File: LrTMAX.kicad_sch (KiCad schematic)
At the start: 126 parts, among them J1 USB_C_Receptacle_USB2.0, J2 Conn_02x05_Odd_Even, Q1 2N7002, SW1 Tact_SW_8mm, SW10 EC11_SMD, SW11 EC11_SMD, SW12 EC11_SMD, SW13 EC11_SMD, SW14 EC11_SMD, SW15 EC11_SMD, SW16 EC11_SMD, SW17 EC11_SMD, SW2 Tact_SW_8mm, SW20 SW_SPST, SW3 Tact_SW_8mm, SW4 Tact_SW_8mm, SW5 Tact_SW_8mm, SW6 Tact_SW_8mm, SW7 Tact_SW_8mm, SW8 Tact_SW_8mm, U1 STM32F072C8Tx, U3 SSD1306_OLED_0.91, U4 SPX3819M5-L3-3TR

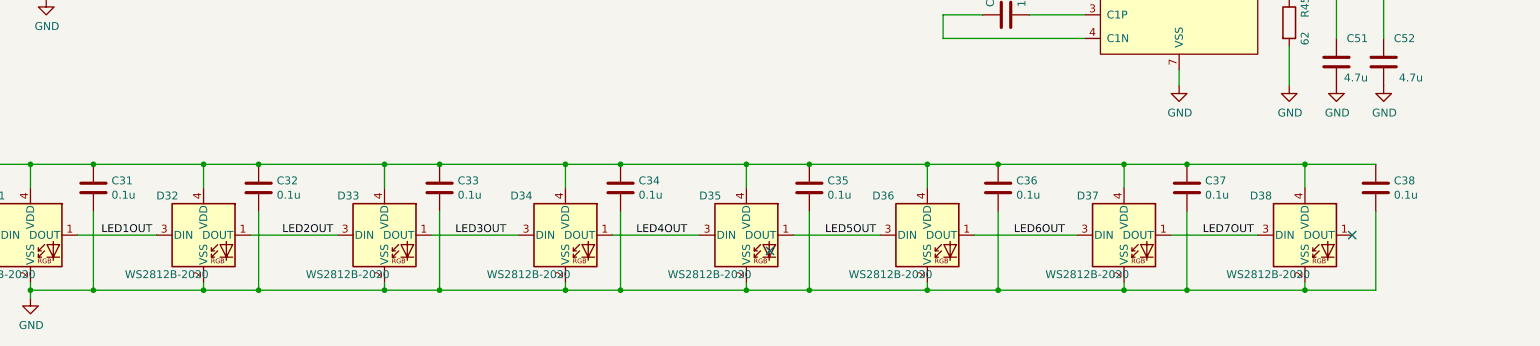
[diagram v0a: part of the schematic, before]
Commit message: change schematic 0.1->100n
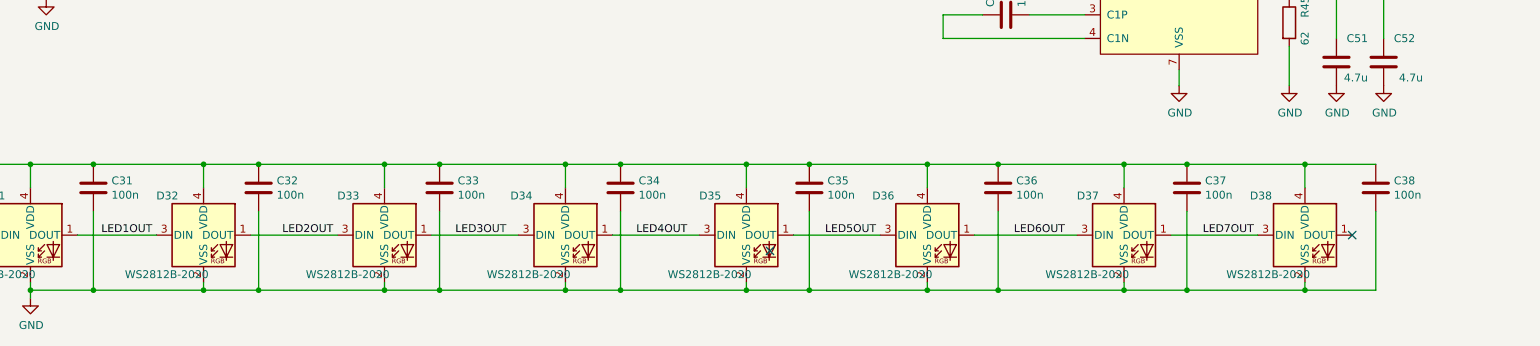
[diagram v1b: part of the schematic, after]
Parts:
- C31, C32, C33, C34, C35, C36, C37, C38: value 0.1u -> 100n
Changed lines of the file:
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@@
       (effects (font (size 1.27 1.27)) (justify left))
     )
-    (property "Value" "0.1u" (id 1) (at 53.721 262.763 0)
+    (property "Value" "100n" (id 1) (at 53.721 262.763 0)
       (effects (font (size 1.27 1.27)) (justify left))
     )
@@
       (effects (font (size 1.27 1.27)) (justify left))
     )
-    (property "Value" "0.1u" (id 1) (at 80.391 262.763 0)
+    (property "Value" "100n" (id 1) (at 80.391 262.763 0)
       (effects (font (size 1.27 1.27)) (justify left))
     )
@@
       (effects (font (size 1.27 1.27)) (justify left))
     )
-    (property "Value" "0.1u" (id 1) (at 109.601 262.763 0)
+    (property "Value" "100n" (id 1) (at 109.601 262.763 0)
       (effects (font (size 1.27 1.27)) (justify left))
     )
@@
       (effects (font (size 1.27 1.27)) (justify left))
     )
-    (property "Value" "0.1u" (id 1) (at 138.811 262.763 0)
+    (property "Value" "100n" (id 1) (at 138.811 262.763 0)
       (effects (font (size 1.27 1.27)) (justify left))
     )
@@
       (effects (font (size 1.27 1.27)) (justify left))
     )
-    (property "Value" "0.1u" (id 1) (at 169.291 262.763 0)
+    (property "Value" "100n" (id 1) (at 169.291 262.763 0)
       (effects (font (size 1.27 1.27)) (justify left))
     )
@@
       (effects (font (size 1.27 1.27)) (justify left))
     )
-    (property "Value" "0.1u" (id 1) (at 199.771 262.763 0)
+    (property "Value" "100n" (id 1) (at 199.771 262.763 0)
       (effects (font (size 1.27 1.27)) (justify left))
     )
@@
       (effects (font (size 1.27 1.27)) (justify left))
     )
-    (property "Value" "0.1u" (id 1) (at 230.251 262.763 0)
+    (property "Value" "100n" (id 1) (at 230.251 262.763 0)
       (effects (font (size 1.27 1.27)) (justify left))
     )
@@
       (effects (font (size 1.27 1.27)) (justify left))
     )
-    (property "Value" "0.1u" (id 1) (at 260.731 262.763 0)
+    (property "Value" "100n" (id 1) (at 260.731 262.763 0)
       (effects (font (size 1.27 1.27)) (justify left))
     )
@@
     )
     (path "/00000000-0000-0000-0000-00005d7055e7"
-      (reference "C31") (unit 1) (value "0.1u") (footprint "Capacitor_SMD:C_0805_2012Metric")
+      (reference "C31") (unit 1) (value "100n") (footprint "Capacitor_SMD:C_0805_2012Metric")
     )
     (path "/00000000-0000-0000-0000-00005d706229"
-      (reference "C32") (unit 1) (value "0.1u") (footprint "Capacitor_SMD:C_0805_2012Metric")
+      (reference "C32") (unit 1) (value "100n") (footprint "Capacitor_SMD:C_0805_2012Metric")
     )
     (path "/00000000-0000-0000-0000-00005d706b4b"
-      (reference "C33") (unit 1) (value "0.1u") (footprint "Capacitor_SMD:C_0805_2012Metric")
+      (reference "C33") (unit 1) (value "100n") (footprint "Capacitor_SMD:C_0805_2012Metric")
     )
     (path "/00000000-0000-0000-0000-00005d707270"
-      (reference "C34") (unit 1) (value "0.1u") (footprint "Capacitor_SMD:C_0805_2012Metric")
+      (reference "C34") (unit 1) (value "100n") (footprint "Capacitor_SMD:C_0805_2012Metric")
     )
     (path "/00000000-0000-0000-0000-00005d7076c0"
-      (reference "C35") (unit 1) (value "0.1u") (footprint "Capacitor_SMD:C_0805_2012Metric")
+      (reference "C35") (unit 1) (value "100n") (footprint "Capacitor_SMD:C_0805_2012Metric")
     )
     (path "/00000000-0000-0000-0000-00005d708e26"
-      (reference "C36") (unit 1) (value "0.1u") (footprint "Capacitor_SMD:C_0805_2012Metric")
+      (reference "C36") (unit 1) (value "100n") (footprint "Capacitor_SMD:C_0805_2012Metric")
     )
     (path "/00000000-0000-0000-0000-000060809be9"
-      (reference "C37") (unit 1) (value "0.1u") (footprint "Capacitor_SMD:C_0805_2012Metric")
+      (reference "C37") (unit 1) (value "100n") (footprint "Capacitor_SMD:C_0805_2012Metric")
     )
     (path "/00000000-0000-0000-0000-000060809bf1"
-      (reference "C38") (unit 1) (value "0.1u") (footprint "Capacitor_SMD:C_0805_2012Metric")
+      (reference "C38") (unit 1) (value "100n") (footprint "Capacitor_SMD:C_0805_2012Metric")
     )
     (path "/00000000-0000-0000-0000-00005c490efe"

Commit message: some pattern/sylk refinement
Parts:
- C10, C11, C12, C13, C14, C15, C16, C17, C18, C19, C20, C21, C22, C23, C24, C25: value 22n -> 33n
- H1, H2, H3, H4: now left out of the parts list
- R48: value 1K -> 470
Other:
- note added: "LrTMAX type C/DFU/SSM"
- note removed: "LrTMAX type C/DFU"
- title: LrTMAX 1.2d -> LrTMAX 1.2
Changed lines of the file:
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@@
   (paper "A3")
   (title_block
-    (title "LrTMAX 1.2d")
+    (title "LrTMAX 1.2")
     (date "2019-01-24")
     (company "Ruffles Inc,.")
@@
     (stroke (width 0) (type default) (color 0 0 0 0))
   )
-  (text "LrTMAX type C/DFU" (at 330.2 265.43 0)
+  (text "LrTMAX type C/DFU/SSM" (at 308.61 264.16 0)
     (effects (font (size 5.0038 5.0038)) (justify left bottom))
   )
@@
   )
   (symbol (lib_id "LrE-6-rescue:MountingHole-Mechanical") (at 307.34 247.65 0) (unit 1)
-    (in_bom yes) (on_board yes)
+    (in_bom no) (on_board yes)
     (property "Reference" "H1" (id 0) (at 309.88 246.4816 0)
       (effects (font (size 1.27 1.27)) (justify left))
@@
   )
   (symbol (lib_id "LrE-6-rescue:MountingHole-Mechanical") (at 328.93 247.65 0) (unit 1)
-    (in_bom yes) (on_board yes)
+    (in_bom no) (on_board yes)
     (property "Reference" "H2" (id 0) (at 331.47 246.4816 0)
       (effects (font (size 1.27 1.27)) (justify left))
@@
   )
   (symbol (lib_id "LrE-6-rescue:MountingHole-Mechanical") (at 349.25 247.65 0) (unit 1)
-    (in_bom yes) (on_board yes)
+    (in_bom no) (on_board yes)
     (property "Reference" "H3" (id 0) (at 351.79 246.4816 0)
       (effects (font (size 1.27 1.27)) (justify left))
@@
   )
   (symbol (lib_id "LrE-6-rescue:MountingHole-Mechanical") (at 370.84 247.65 0) (unit 1)
-    (in_bom yes) (on_board yes)
+    (in_bom no) (on_board yes)
     (property "Reference" "H4" (id 0) (at 373.38 246.4816 0)
       (effects (font (size 1.27 1.27)) (justify left))
@@
     (in_bom yes) (on_board yes)
     (property "Reference" "R48" (id 0) (at 60.96 205.5622 90))
-    (property "Value" "1K" (id 1) (at 60.96 207.8736 90))
+    (property "Value" "470" (id 1) (at 60.96 207.8736 90))
     (property "Footprint" "Resistor_SMD:R_0805_2012Metric" (id 2) (at 60.96 209.042 90)
       (effects (font (size 1.27 1.27)) hide)
@@
       (effects (font (size 1.27 1.27)) (justify left))
     )
-    (property "Value" "22n" (id 1) (at 40.64 90.17 0)
+    (property "Value" "33n" (id 1) (at 40.64 90.17 0)
       (effects (font (size 1.27 1.27)) (justify left))
     )
@@
       (effects (font (size 1.27 1.27)) (justify left))
     )
-    (property "Value" "22n" (id 1) (at 49.53 90.17 0)
+    (property "Value" "33n" (id 1) (at 49.53 90.17 0)
       (effects (font (size 1.27 1.27)) (justify left))
     )
@@
       (effects (font (size 1.27 1.27)) (justify left))
     )
-    (property "Value" "22n" (id 1) (at 39.37 132.08 0)
+    (property "Value" "33n" (id 1) (at 39.37 132.08 0)
       (effects (font (size 1.27 1.27)) (justify left))
     )
@@
       (effects (font (size 1.27 1.27)) (justify left))
     )
-    (property "Value" "22n" (id 1) (at 48.26 132.08 0)
+    (property "Value" "33n" (id 1) (at 48.26 132.08 0)
       (effects (font (size 1.27 1.27)) (justify left))
     )
@@
       (effects (font (size 1.27 1.27)) (justify left))
     )
-    (property "Value" "22n" (id 1) (at 111.76 48.26 0)
+    (property "Value" "33n" (id 1) (at 111.76 48.26 0)
       (effects (font (size 1.27 1.27)) (justify left))
     )
@@
       (effects (font (size 1.27 1.27)) (justify left))
     )
-    (property "Value" "22n" (id 1) (at 120.65 48.26 0)
+    (property "Value" "33n" (id 1) (at 120.65 48.26 0)
       (effects (font (size 1.27 1.27)) (justify left))
     )
@@
       (effects (font (size 1.27 1.27)) (justify left))
     )
-    (property "Value" "22n" (id 1) (at 114.3 91.44 0)
+    (property "Value" "33n" (id 1) (at 114.3 91.44 0)
       (effects (font (size 1.27 1.27)) (justify left))
     )
@@
       (effects (font (size 1.27 1.27)) (justify left))
     )
-    (property "Value" "22n" (id 1) (at 123.19 91.44 0)
+    (property "Value" "33n" (id 1) (at 123.19 91.44 0)
       (effects (font (size 1.27 1.27)) (justify left))
     )
@@
       (effects (font (size 1.27 1.27)) (justify left))
     )
-    (property "Value" "22n" (id 1) (at 40.64 46.99 0)
+    (property "Value" "33n" (id 1) (at 40.64 46.99 0)
       (effects (font (size 1.27 1.27)) (justify left))
     )
@@
       (effects (font (size 1.27 1.27)) (justify left))
     )
-    (property "Value" "22n" (id 1) (at 50.8 46.99 0)
+    (property "Value" "33n" (id 1) (at 50.8 46.99 0)
       (effects (font (size 1.27 1.27)) (justify left))
     )
@@
       (effects (font (size 1.27 1.27)) (justify left))
     )
-    (property "Value" "22n" (id 1) (at 43.18 176.53 0)
+    (property "Value" "33n" (id 1) (at 43.18 176.53 0)
       (effects (font (size 1.27 1.27)) (justify left))
     )
@@
       (effects (font (size 1.27 1.27)) (justify left))
     )
-    (property "Value" "22n" (id 1) (at 50.8 176.53 0)
+    (property "Value" "33n" (id 1) (at 50.8 176.53 0)
       (effects (font (size 1.27 1.27)) (justify left))
     )
@@
       (effects (font (size 1.27 1.27)) (justify left))
     )
-    (property "Value" "22n" (id 1) (at 114.3 177.8 0)
+    (property "Value" "33n" (id 1) (at 114.3 177.8 0)
       (effects (font (size 1.27 1.27)) (justify left))
     )
@@
       (effects (font (size 1.27 1.27)) (justify left))
     )
-    (property "Value" "22n" (id 1) (at 124.46 177.8 0)
+    (property "Value" "33n" (id 1) (at 124.46 177.8 0)
       (effects (font (size 1.27 1.27)) (justify left))
     )
@@
       (effects (font (size 1.27 1.27)) (justify left))
     )
-    (property "Value" "22n" (id 1) (at 115.57 134.62 0)
+    (property "Value" "33n" (id 1) (at 115.57 134.62 0)
       (effects (font (size 1.27 1.27)) (justify left))
     )
@@
       (effects (font (size 1.27 1.27)) (justify left))
     )
-    (property "Value" "22n" (id 1) (at 123.19 134.62 0)
+    (property "Value" "33n" (id 1) (at 123.19 134.62 0)
       (effects (font (size 1.27 1.27)) (justify left))
     )
@@
     )
     (path "/00000000-0000-0000-0000-00005c92acd6"
-      (reference "C10") (unit 1) (value "22n") (footprint "Capacitor_SMD:C_0805_2012Metric")
+      (reference "C10") (unit 1) (value "33n") (footprint "Capacitor_SMD:C_0805_2012Metric")
     )
     (path "/00000000-0000-0000-0000-00005c92ade4"
-      (reference "C11") (unit 1) (value "22n") (footprint "Capacitor_SMD:C_0805_2012Metric")
+      (reference "C11") (unit 1) (value "33n") (footprint "Capacitor_SMD:C_0805_2012Metric")
     )
     (path "/00000000-0000-0000-0000-00005c8cf4fd"
-      (reference "C12") (unit 1) (value "22n") (footprint "Capacitor_SMD:C_0805_2012Metric")
+      (reference "C12") (unit 1) (value "33n") (footprint "Capacitor_SMD:C_0805_2012Metric")
     )
     (path "/00000000-0000-0000-0000-00005c8cf611"
-      (reference "C13") (unit 1) (value "22n") (footprint "Capacitor_SMD:C_0805_2012Metric")
+      (reference "C13") (unit 1) (value "33n") (footprint "Capacitor_SMD:C_0805_2012Metric")
     )
     (path "/00000000-0000-0000-0000-00005c8cf744"
-      (reference "C14") (unit 1) (value "22n") (footprint "Capacitor_SMD:C_0805_2012Metric")
+      (reference "C14") (unit 1) (value "33n") (footprint "Capacitor_SMD:C_0805_2012Metric")
     )
     (path "/00000000-0000-0000-0000-00005c8cf86c"
-      (reference "C15") (unit 1) (value "22n") (footprint "Capacitor_SMD:C_0805_2012Metric")
+      (reference "C15") (unit 1) (value "33n") (footprint "Capacitor_SMD:C_0805_2012Metric")
     )
     (path "/00000000-0000-0000-0000-00005c92aef7"
-      (reference "C16") (unit 1) (value "22n") (footprint "Capacitor_SMD:C_0805_2012Metric")
+      (reference "C16") (unit 1) (value "33n") (footprint "Capacitor_SMD:C_0805_2012Metric")
     )
     (path "/00000000-0000-0000-0000-00005c92b0b3"
-      (reference "C17") (unit 1) (value "22n") (footprint "Capacitor_SMD:C_0805_2012Metric")
+      (reference "C17") (unit 1) (value "33n") (footprint "Capacitor_SMD:C_0805_2012Metric")
     )
     (path "/00000000-0000-0000-0000-00005c92a85a"
-      (reference "C18") (unit 1) (value "22n") (footprint "Capacitor_SMD:C_0805_2012Metric")
+      (reference "C18") (unit 1) (value "33n") (footprint "Capacitor_SMD:C_0805_2012Metric")
     )
     (path "/00000000-0000-0000-0000-00005c92a94c"
-      (reference "C19") (unit 1) (value "22n") (footprint "Capacitor_SMD:C_0805_2012Metric")
+      (reference "C19") (unit 1) (value "33n") (footprint "Capacitor_SMD:C_0805_2012Metric")
     )
     (path "/00000000-0000-0000-0000-00005c92aa33"
-      (reference "C20") (unit 1) (value "22n") (footprint "Capacitor_SMD:C_0805_2012Metric")
+      (reference "C20") (unit 1) (value "33n") (footprint "Capacitor_SMD:C_0805_2012Metric")
     )
     (path "/00000000-0000-0000-0000-00005c92abb3"
-      (reference "C21") (unit 1) (value "22n") (footprint "Capacitor_SMD:C_0805_2012Metric")
+      (reference "C21") (unit 1) (value "33n") (footprint "Capacitor_SMD:C_0805_2012Metric")
     )
     (path "/00000000-0000-0000-0000-000060a9284f"
-      (reference "C22") (unit 1) (value "22n") (footprint "Capacitor_SMD:C_0805_2012Metric")
+      (reference "C22") (unit 1) (value "33n") (footprint "Capacitor_SMD:C_0805_2012Metric")
     )
     (path "/00000000-0000-0000-0000-000060a92855"
-      (reference "C23") (unit 1) (value "22n") (footprint "Capacitor_SMD:C_0805_2012Metric")
+      (reference "C23") (unit 1) (value "33n") (footprint "Capacitor_SMD:C_0805_2012Metric")
     )
     (path "/00000000-0000-0000-0000-000060a92843"
-      (reference "C24") (unit 1) (value "22n") (footprint "Capacitor_SMD:C_0805_2012Metric")
+      (reference "C24") (unit 1) (value "33n") (footprint "Capacitor_SMD:C_0805_2012Metric")
     )
     (path "/00000000-0000-0000-0000-000060a92849"
-      (reference "C25") (unit 1) (value "22n") (footprint "Capacitor_SMD:C_0805_2012Metric")
+      (reference "C25") (unit 1) (value "33n") (footprint "Capacitor_SMD:C_0805_2012Metric")
     )
     (path "/00000000-0000-0000-0000-00005d54b231"
@@
     )
     (path "/00000000-0000-0000-0000-00005c5249ab"
-      (reference "R48") (unit 1) (value "1K") (footprint "Resistor_SMD:R_0805_2012Metric")
+      (reference "R48") (unit 1) (value "470") (footprint "Resistor_SMD:R_0805_2012Metric")
     )
     (path "/00000000-0000-0000-0000-00005cce212b"
